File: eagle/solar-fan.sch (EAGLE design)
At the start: 36 parts, among them J1 POWER_JACKPTH, J2 USB-A-S, J3 7805, U1 LT3652, U2 ATTINY85

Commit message: first draft of board layout, minor schematic fixes
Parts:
- added J5: (no value), SparkFun-Connectors:M02JST-PTH-2
- added R13, R14, R15: 100k, SparkFun-Passives:RESISTOR0603-RES
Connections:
- removed net N$10: C5.+
- new net N$1: Q1.B, R13.2
- new net N$2: Q2.B, R14.2
- new net N$3: Q3.B, R15.2
- net FAN_OUT: now also R15.1, U2.2; no longer Q3.B, U2.0
- net GND: now also J5.2
- net LED_OUT: now also R13.1; no longer Q1.B
- net USB_OUT: now also R14.1, U2.0; no longer Q2.B, U2.2
- net V_BATT: now also C5.+, J5.1
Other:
- moved on the sheet: D4, D5, D6, D7, D8, D9, J2, J4, Q1, Q2, Q3, R11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

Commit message: minor layout updates, adding PNs to schematic
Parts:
- D1: PN (none) -> MBRS140FSCT-ND
- D4, D5, D6, D7, D8, D9: PN (none) -> 516-2236-1-ND
- J1: PN (none) -> CP-202A-ND
- J4: device SparkFun-Connectors:M02PTH -> SparkFun-Connectors:M02POLAR
- Q1, Q2, Q3: PN (none) -> PN2222AFS-ND
- R1: PN (none) -> P499KHCT-ND
- R10, R13, R14, R15, R2, R4: PN (none) -> P100KHCT-ND
- R11, R12: PN (none) -> P100HCT-ND
- R5: PN (none) -> P174KHCT-ND
- R7, R8: PN (none) -> 3386U-1-103LF-ND
- R9: PN (none) -> P309KHCT-ND
- U1: PN (none) -> LT3652EMSE#PBF-ND
- U2: PN (none) -> ATTINY85-20PU-ND

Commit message: layout update, bom, components
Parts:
- removed J2: USB-A-S, SparkFun-Connectors:USB-A-S
- added C6: 0.1uf, SparkFun-Passives:CAP0603-CAP
- added C7: 0.33uf, SparkFun-Passives:CAP0603-CAP
- added J6: USB_, SparkFun-Connectors:USB_
- C1, C4: PN (none) -> 490-1880-1-ND
- C2: PN (none) -> 490-10481-1-ND
- C3: PN (none) -> 490-1536-1-ND
- C5: PN (none) -> 399-6650-1-ND
- D1: PN MBRS140FSCT-ND -> MBRS140T3GOSCT-ND
- D2: PN (none) -> SZBZX84C6V2LT1GOSCT-ND
- D3: PN (none) -> MBRS340T3GOSTR-ND
- D4, D5, D6, D7, D8, D9: PN 516-2236-1-ND -> 1516-1057-1-ND
- J3: PN (none) -> LM7805CT-ND
- J4: PN (none) -> WM4200-ND
- J5: PN (none) -> 455-1719-ND
- L1: PN (none) -> RLB0912-220KL-ND
- R3: PN (none) -> P309KHCT-ND
- R6: PN (none) -> 1276-6155-1-ND
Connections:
- removed net N$22: J4.2, Q3.C
- new net N$6: J4.1, Q3.C
- net 5V: now also C6.1, J6.VBUS; no longer J2.VBUS
- net GND: now also C6.2, C7.2, J5.1; no longer J5.2
- net N$20: now also J6.D+, J6.D-; no longer J2.D+, J2.D-
- net N$21: now also J6.GND; no longer J2.GND
- net V_BATT: now also C7.1, J4.2, J5.2; no longer J4.1, J5.1
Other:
- moved on the sheet: J4, J5, Q2, Q3, R14, R15, R7, R8, R9

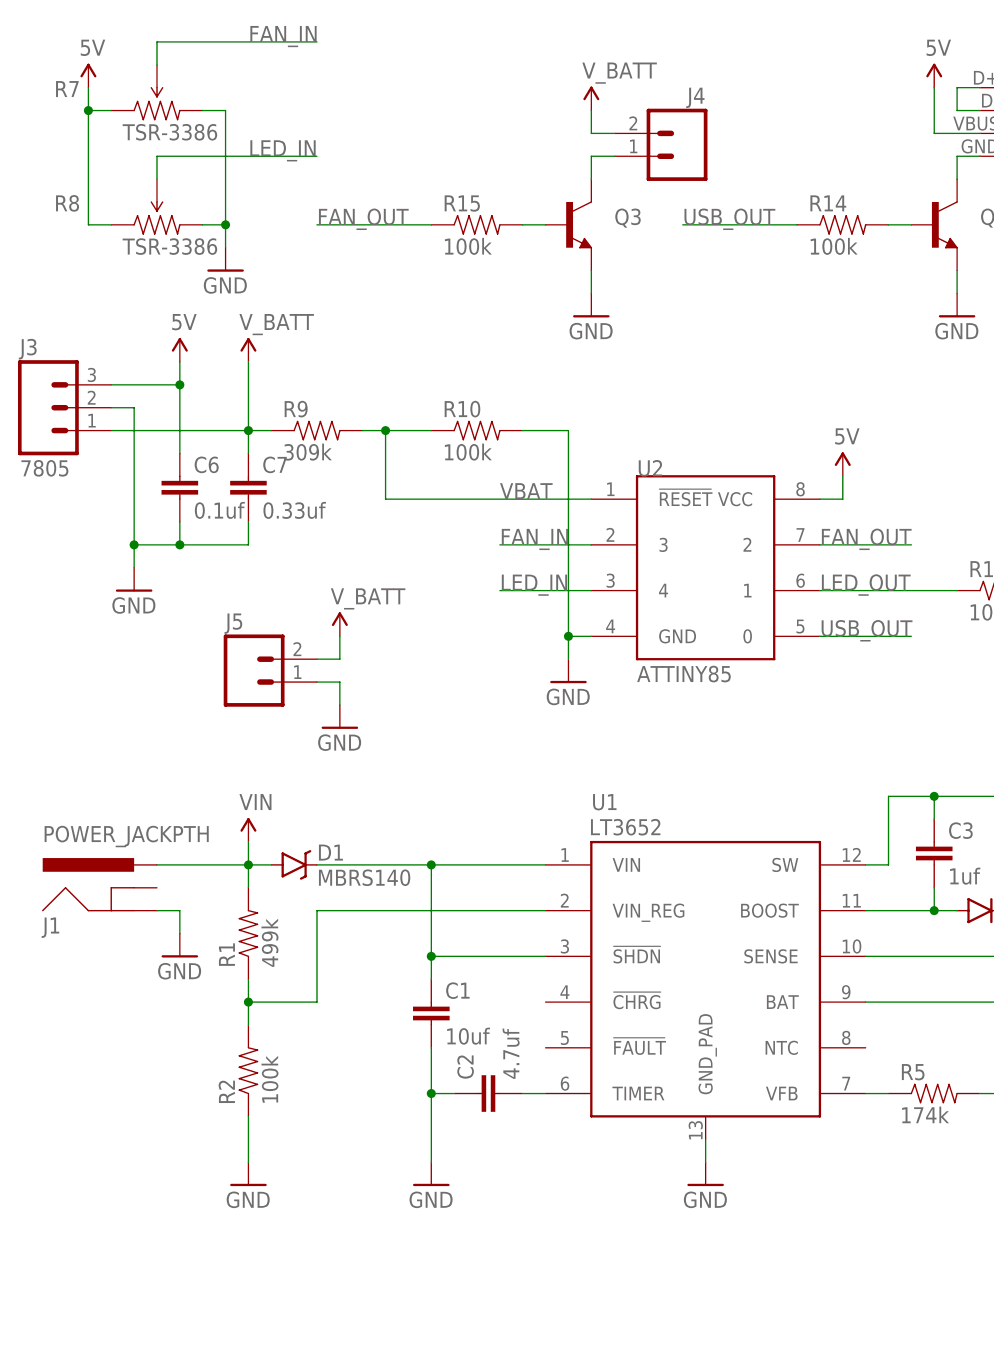
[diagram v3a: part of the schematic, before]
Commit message: updated fan connector and layout, silk screen, mfg files
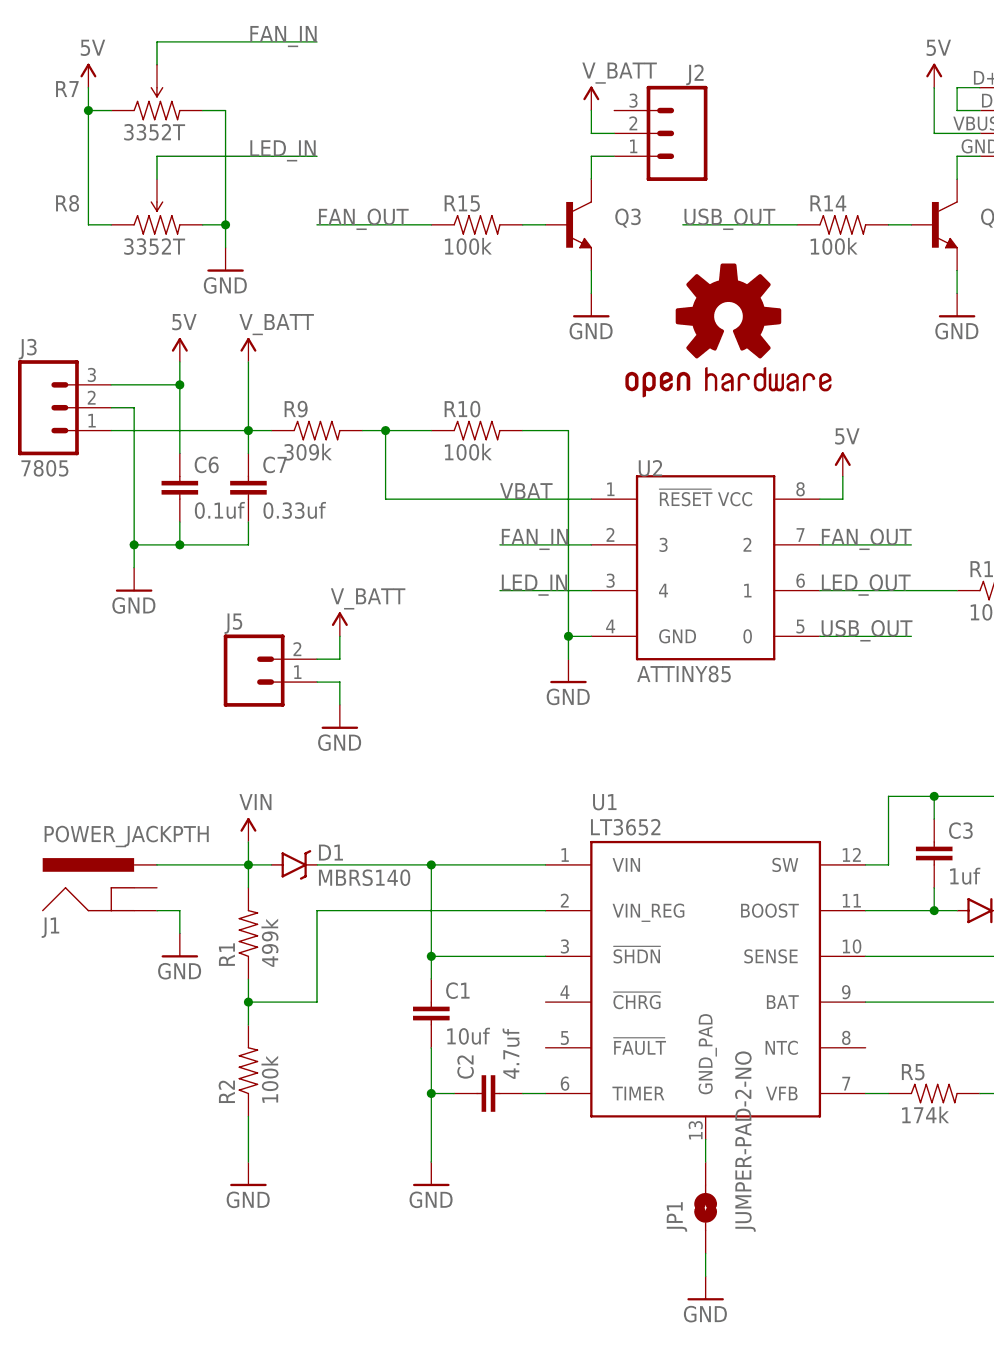
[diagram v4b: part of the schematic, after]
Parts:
- removed J4: (no value), SparkFun-Connectors:M02POLAR
- added J2: (no value), SparkFun-Connectors:M03POLAR
- added JP1: JUMPER-PAD-2-NO, SparkFun-Passives:JUMPER-PAD-2-NO
- added LOGO1: OSHW-LOGOMINI, SparkFun-Aesthetics:OSHW-LOGOMINI
- R7, R8: value TSR-3386 -> 3352T; device SparkFun-Electromechanical:TRIMPOT-PTH-KNOB -> bourns3352:3352T; PN 3386U-1-103LF-ND -> 3352T-103LF-ND
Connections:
- new net PAD: JP1.2, U1.GND_PAD
- net GND: now also JP1.1; no longer U1.GND_PAD
- net N$6: now also J2.1; no longer J4.1
- net V_BATT: now also J2.2; no longer J4.2
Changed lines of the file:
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@@
 <layer number="19" name="Unrouted" color="6" fill="1" visible="yes" active="no"/>
 <layer number="20" name="Dimension" color="15" fill="1" visible="yes" active="no"/>
-<layer number="21" name="tPlace" color="7" fill="1" visible="yes" active="no"/>
-<layer number="22" name="bPlace" color="7" fill="1" visible="yes" active="no"/>
+<layer number="21" name="tPlace" color="14" fill="1" visible="yes" active="no"/>
+<layer number="22" name="bPlace" color="14" fill="1" visible="yes" active="no"/>
 <layer number="23" name="tOrigins" color="15" fill="1" visible="yes" active="no"/>
 <layer number="24" name="bOrigins" color="15" fill="1" visible="yes" active="no"/>
@@
 <layer number="49" name="Reference" color="7" fill="1" visible="yes" active="no"/>
 <layer number="50" name="dxf" color="7" fill="1" visible="yes" active="no"/>
-<layer number="51" name="tDocu" color="7" fill="1" visible="yes" active="no"/>
-<layer number="52" name="bDocu" color="7" fill="1" visible="yes" active="no"/>
+<layer number="51" name="tDocu" color="14" fill="1" visible="yes" active="no"/>
+<layer number="52" name="bDocu" color="14" fill="1" visible="yes" active="no"/>
 <layer number="53" name="tGND_GNDA" color="7" fill="9" visible="yes" active="no"/>
 <layer number="54" name="bGND_GNDA" color="1" fill="9" visible="yes" active="no"/>
@@
 <part name="SUPPLY5" library="SparkFun-Aesthetics" deviceset="5V" device=""/>
 <part name="GND8" library="SparkFun-Aesthetics" deviceset="GND" device=""/>
-<part name="R7" library="SparkFun-Electromechanical" deviceset="TRIMPOT" device="-PTH-KNOB" value="TSR-3386">
-<attribute name="PN" value="3386U-1-103LF-ND"/>
-</part>
-<part name="R8" library="SparkFun-Electromechanical" deviceset="TRIMPOT" device="-PTH-KNOB" value="TSR-3386">
-<attribute name="PN" value="3386U-1-103LF-ND"/>
-</part>
 <part name="SUPPLY6" library="SparkFun-Aesthetics" deviceset="5V" device=""/>
 <part name="GND9" library="SparkFun-Aesthetics" deviceset="GND" device=""/>
@@
 <part name="SUPPLY10" library="SparkFun-Aesthetics" deviceset="V_BATT" device=""/>
 <part name="GND13" library="SparkFun-Aesthetics" deviceset="GND" device=""/>
-<part name="J4" library="SparkFun-Connectors" deviceset="M02" device="POLAR">
-<attribute name="PN" value="WM4200-ND"/>
-</part>
 <part name="C6" library="SparkFun-Passives" deviceset="CAP" device="0603-CAP" value="0.1uf">
 <attribute name="PN" value="490-1532-1-ND"/>
@@
 <part name="J6" library="SparkFun-Connectors" deviceset="USB" device="_">
 <attribute name="PN" value="1175-1001-ND"/>
+</part>
+<part name="JP1" library="SparkFun-Passives" deviceset="JUMPER-PAD-2-NO" device=""/>
+<part name="R7" library="bourns3352" deviceset="3352T" device="">
+<attribute name="PN" value="3352T-103LF-ND"/>
+</part>
+<part name="R8" library="bourns3352" deviceset="3352T" device="">
+<attribute name="PN" value="3352T-103LF-ND"/>
+</part>
+<part name="LOGO1" library="SparkFun-Aesthetics" deviceset="OSHW-LOGO" device="MINI" value="OSHW-LOGOMINI"/>
+<part name="J2" library="SparkFun-Connectors" deviceset="M03" device="POLAR">
+<attribute name="PN" value="WM4201-ND"/>
 </part>
 </parts>
@@
 <instance part="SUPPLY1" gate="G$1" x="58.42" y="109.22"/>
 <instance part="GND2" gate="1" x="78.74" y="71.12"/>
-<instance part="GND3" gate="1" x="109.22" y="71.12"/>
+<instance part="GND3" gate="1" x="109.22" y="58.42"/>
 <instance part="C3" gate="G$1" x="134.62" y="106.68">
 <attribute name="PN" x="134.62" y="106.68" size="1.778" layer="96" display="off"/>
@@
 <instance part="SUPPLY5" gate="G$1" x="124.46" y="149.86"/>
 <instance part="GND8" gate="1" x="93.98" y="127"/>
-<instance part="R7" gate="R?" x="48.26" y="190.5">
-<attribute name="PN" x="48.26" y="190.5" size="1.778" layer="96" display="off"/>
-</instance>
-<instance part="R8" gate="R?" x="48.26" y="177.8">
-<attribute name="PN" x="48.26" y="177.8" size="1.778" layer="96" display="off"/>
-</instance>
 <instance part="SUPPLY6" gate="G$1" x="40.64" y="193.04"/>
 <instance part="GND9" gate="1" x="55.88" y="172.72"/>
@@
 <instance part="SUPPLY10" gate="G$1" x="68.58" y="132.08"/>
 <instance part="GND13" gate="1" x="68.58" y="121.92"/>
-<instance part="J4" gate="G$1" x="106.68" y="185.42" rot="MR0">
-<attribute name="PN" x="106.68" y="185.42" size="1.778" layer="96" rot="MR0" display="off"/>
-</instance>
 <instance part="C6" gate="G$1" x="50.8" y="147.32">
 <attribute name="PN" x="50.8" y="147.32" size="1.778" layer="96" display="off"/>
@@
 <instance part="J6" gate="G$1" x="142.24" y="185.42">
 <attribute name="PN" x="142.24" y="185.42" size="1.778" layer="96" display="off"/>
+</instance>
+<instance part="JP1" gate="G$1" x="109.22" y="68.58" rot="R90"/>
+<instance part="R7" gate="G$1" x="48.26" y="190.5">
+<attribute name="PN" x="48.26" y="190.5" size="1.778" layer="96" display="off"/>
+</instance>
+<instance part="R8" gate="G$1" x="48.26" y="177.8">
+<attribute name="PN" x="48.26" y="177.8" size="1.778" layer="96" display="off"/>
+</instance>
+<instance part="LOGO1" gate="G$1" x="111.76" y="167.64"/>
+<instance part="J2" gate="J$1" x="106.68" y="187.96" rot="MR0">
+<attribute name="PN" x="106.68" y="187.96" size="1.778" layer="96" rot="MR0" display="off"/>
 </instance>
 </instances>
@@
 <wire x1="81.28" y1="81.28" x2="78.74" y2="81.28" width="0.1524" layer="91"/>
 <junction x="78.74" y="81.28"/>
-</segment>
-<segment>
-<pinref part="U1" gate="G$1" pin="GND_PAD"/>
-<pinref part="GND3" gate="1" pin="GND"/>
-<wire x1="109.22" y1="76.2" x2="109.22" y2="73.66" width="0.1524" layer="91"/>
 </segment>
 <segment>
@@
 </segment>
 <segment>
-<pinref part="R8" gate="R?" pin="CW"/>
 <pinref part="GND9" gate="1" pin="GND"/>
 <wire x1="53.34" y1="177.8" x2="55.88" y2="177.8" width="0.1524" layer="91"/>
 <wire x1="55.88" y1="177.8" x2="55.88" y2="175.26" width="0.1524" layer="91"/>
-<pinref part="R7" gate="R?" pin="CW"/>
 <wire x1="53.34" y1="190.5" x2="55.88" y2="190.5" width="0.1524" layer="91"/>
 <wire x1="55.88" y1="190.5" x2="55.88" y2="177.8" width="0.1524" layer="91"/>
 <junction x="55.88" y="177.8"/>
+<pinref part="R7" gate="G$1" pin="CW"/>
+<pinref part="R8" gate="G$1" pin="CW"/>
 </segment>
 <segment>
@@
 <wire x1="66.04" y1="127" x2="68.58" y2="127" width="0.1524" layer="91"/>
 <wire x1="68.58" y1="127" x2="68.58" y2="124.46" width="0.1524" layer="91"/>
+</segment>
+<segment>
+<pinref part="JP1" gate="G$1" pin="1"/>
+<pinref part="GND3" gate="1" pin="GND"/>
+<wire x1="109.22" y1="63.5" x2="109.22" y2="60.96" width="0.1524" layer="91"/>
 </segment>
 </net>
@@
 <pinref part="SUPPLY9" gate="G$1" pin="V_BATT"/>
 <wire x1="96.52" y1="190.5" x2="96.52" y2="187.96" width="0.1524" layer="91"/>
-<pinref part="J4" gate="G$1" pin="2"/>
 <wire x1="96.52" y1="187.96" x2="99.06" y2="187.96" width="0.1524" layer="91"/>
+<pinref part="J2" gate="J$1" pin="2"/>
 </segment>
 </net>
@@
 <pinref part="SUPPLY6" gate="G$1" pin="5V"/>
 <wire x1="40.64" y1="193.04" x2="40.64" y2="190.5" width="0.1524" layer="91"/>
-<pinref part="R7" gate="R?" pin="CCW"/>
 <wire x1="40.64" y1="190.5" x2="43.18" y2="190.5" width="0.1524" layer="91"/>
 <wire x1="40.64" y1="190.5" x2="40.64" y2="177.8" width="0.1524" layer="91"/>
-<pinref part="R8" gate="R?" pin="CCW"/>
 <wire x1="40.64" y1="177.8" x2="43.18" y2="177.8" width="0.1524" layer="91"/>
 <junction x="40.64" y="190.5"/>
+<pinref part="R7" gate="G$1" pin="CCW"/>
+<pinref part="R8" gate="G$1" pin="CCW"/>
 </segment>
 <segment>
@@
 <net name="LED_IN" class="0">
 <segment>
-<pinref part="R8" gate="R?" pin="WIPER"/>
 <wire x1="48.26" y1="182.88" x2="48.26" y2="185.42" width="0.1524" layer="91"/>
 <wire x1="48.26" y1="185.42" x2="66.04" y2="185.42" width="0.1524" layer="91"/>
 <label x="58.42" y="185.42" size="1.778" layer="95"/>
+<pinref part="R8" gate="G$1" pin="WIPER"/>
 </segment>
 <segment>
@@
 <net name="FAN_IN" class="0">
 <segment>
-<pinref part="R7" gate="R?" pin="WIPER"/>
 <wire x1="48.26" y1="195.58" x2="48.26" y2="198.12" width="0.1524" layer="91"/>
 <wire x1="48.26" y1="198.12" x2="66.04" y2="198.12" width="0.1524" layer="91"/>
 <label x="58.42" y="198.12" size="1.778" layer="95"/>
+<pinref part="R7" gate="G$1" pin="WIPER"/>
 </segment>
 <segment>
@@
 <pinref part="Q3" gate="G$1" pin="C"/>
 <wire x1="96.52" y1="182.88" x2="96.52" y2="185.42" width="0.1524" layer="91"/>
-<pinref part="J4" gate="G$1" pin="1"/>
 <wire x1="96.52" y1="185.42" x2="99.06" y2="185.42" width="0.1524" layer="91"/>
-</segment>
-</net>
+<pinref part="J2" gate="J$1" pin="1"/>
+</segment>
+</net>
+<net name="PAD" class="0">
+<segment>
+<pinref part="U1" gate="G$1" pin="GND_PAD"/>
+<pinref part="JP1" gate="G$1" pin="2"/>
+<wire x1="109.22" y1="76.2" x2="109.22" y2="73.66" width="0.1524" layer="91"/>
+</segment>
+</net>

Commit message: changed pn for c1 and c4
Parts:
- C1, C4: PN 490-1880-1-ND -> 490-6530-1-ND
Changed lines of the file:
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@@
 </part>
 <part name="C1" library="SparkFun-Passives" deviceset="CAP" device="1210" value="10uf">
-<attribute name="PN" value="490-1880-1-ND"/>
+<attribute name="PN" value="490-6530-1-ND"/>
 </part>
 <part name="C2" library="SparkFun-Passives" deviceset="CAP" device="0603-CAP" value="4.7uf">
@@
 </part>
 <part name="C4" library="SparkFun-Passives" deviceset="CAP" device="1210" value="10uf">
-<attribute name="PN" value="490-1880-1-ND"/>
+<attribute name="PN" value="490-6530-1-ND"/>
 </part>
 <part name="R3" library="SparkFun-Passives" deviceset="RESISTOR" device="0603-RES" value="309k">

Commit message: rev - build
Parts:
- removed LOGO1: OSHW-LOGOMINI, SparkFun-Aesthetics:OSHW-LOGOMINI
- added D10: BZX84C6V2L, SparkFun-DiscreteSemi:BZX84C6V2L
- C1, C4: device SparkFun-Passives:CAP1210 -> SparkFun-Passives:CAP0603-CAP; PN 490-6530-1-ND -> 490-7202-1-ND
- C2: value 4.7uf -> 10uf; PN 490-10481-1-ND -> 490-7202-1-ND
- C6: value 0.1uf -> 10uf; PN 490-1532-1-ND -> 490-7202-1-ND
- C7: value 0.33uf -> 10uf; PN 490-3294-1-ND -> 490-7202-1-ND
- D2: value BZX84C6V2L -> 1N914; device SparkFun-DiscreteSemi:DIODESOT23 -> SparkFun-DiscreteSemi:DIODEBAS16; PN SZBZX84C6V2LT1GOSCT-ND -> 1N914BWSCT-ND
- D3: value MBRS340 -> MBRS140; PN MBRS340T3GOSTR-ND -> MBRS140T3GOSCT-ND
- J3: PN LM7805CT-ND -> 811-2196-5-ND; PN2 (none) -> 811-2196-5-ND
- L1: value 22uH -> 10uH; PN RLB0912-220KL-ND -> RLB0912-100KL-ND
- R13, R14, R15: value 100k -> 390; PN P100KHCT-ND -> P390HCT-ND
- U2: PN2 (none) -> AE9986-ND
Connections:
- removed net N$20: J6.D+, J6.D-
- new net N$10: D10.A, D2.A
- new net N$8: J6.D+, JP1.1
- new net N$9: J6.D-, JP1.2
- net BOOST: now also D2.C; no longer D2.A
- net GND: no longer JP1.1
- net PAD: no longer JP1.2
- net V_BATT: now also D10.C; no longer D2.C
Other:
- moved on the sheet: C1, C2, C3, C4, C5, C6, C7, D1, D2, D3, D4, D5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
